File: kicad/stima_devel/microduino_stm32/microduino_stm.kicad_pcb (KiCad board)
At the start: 2 copper layers, 2 parts, among them IC1 STM32F103CBT6

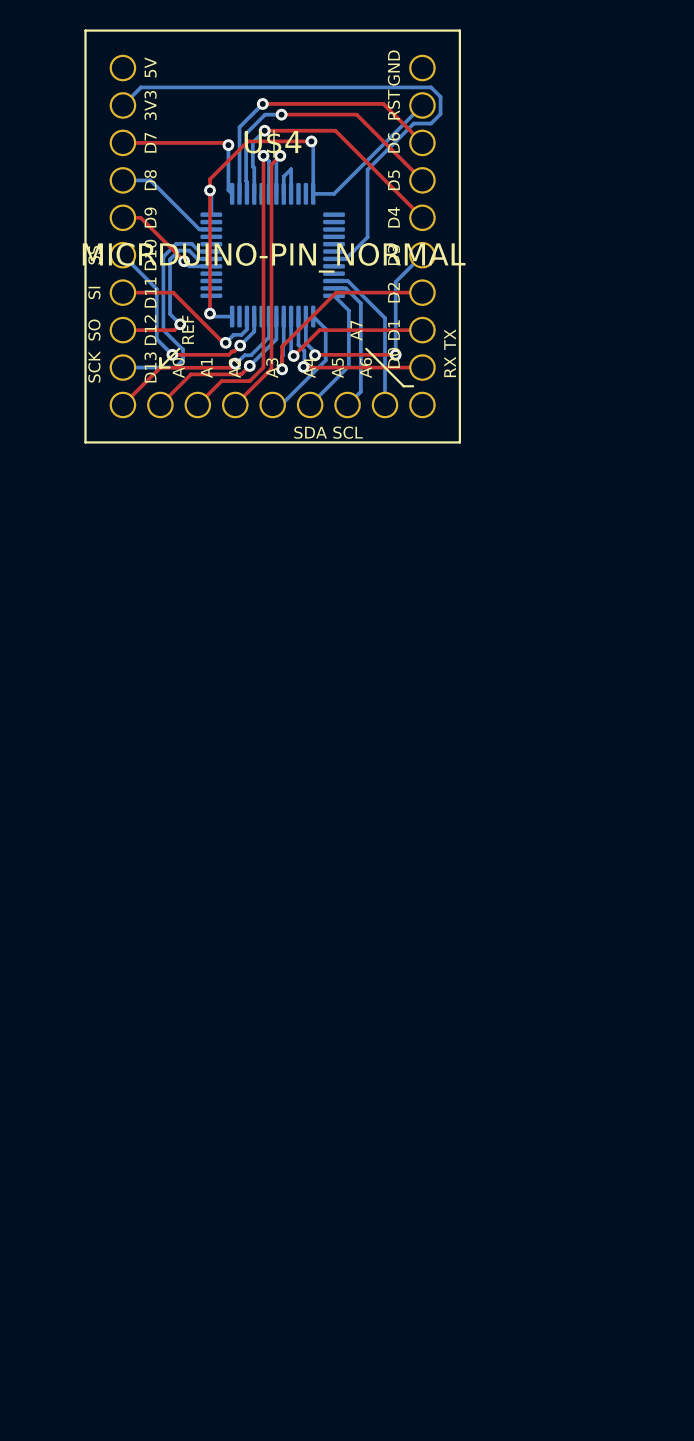
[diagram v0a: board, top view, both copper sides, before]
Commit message: Update schematic and testing partial routing
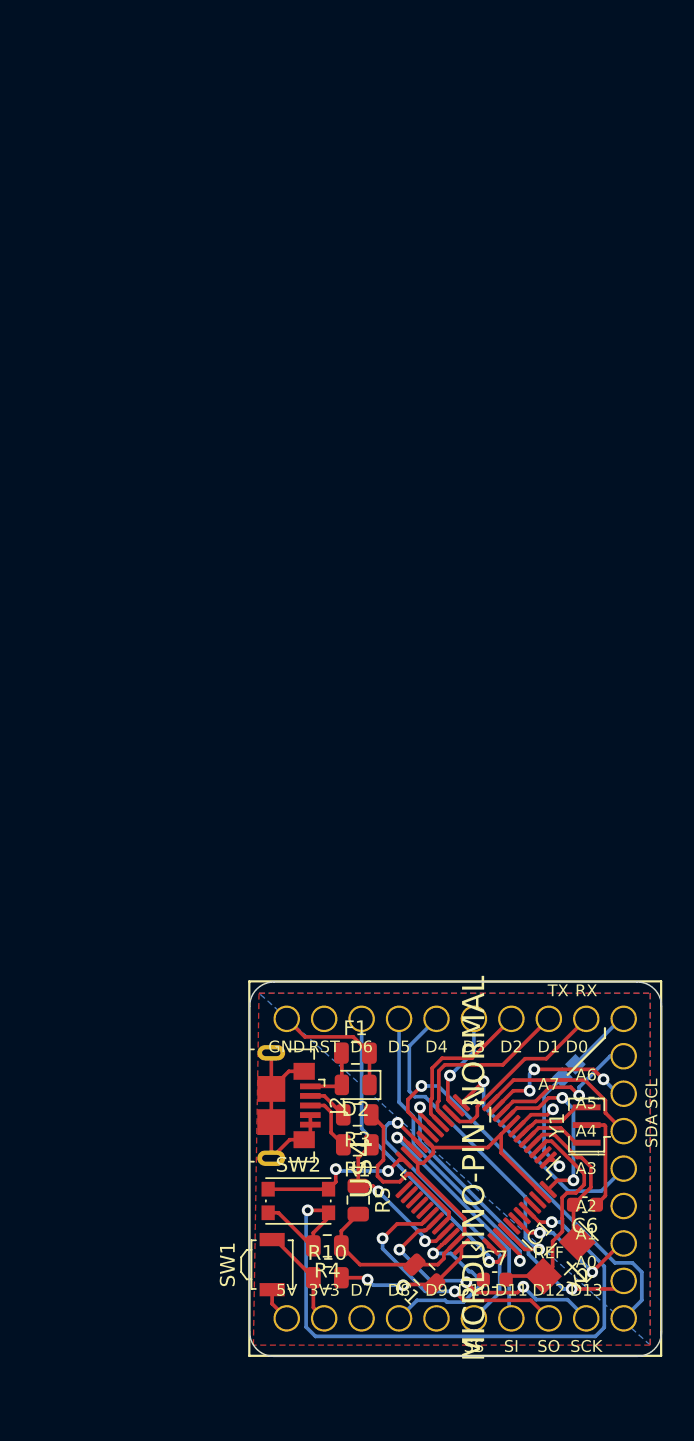
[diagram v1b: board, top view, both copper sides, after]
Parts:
- added C1: 10uF, Capacitor_SMD:C_0805_2012Metric, F.Cu at (158.8, 174.2)
- added C6: 10pF, Capacitor_SMD:C_0603_1608Metric, F.Cu at (169.7, 169.4)
- added C7: 10pF, Capacitor_SMD:C_0603_1608Metric, F.Cu at (163.6, 174.5)
- added D2: D, Diode_SMD:D_0805_2012Metric, F.Cu at (154.1, 161.3)
- added F1: 10uF, Capacitor_SMD:C_0805_2012Metric, F.Cu at (154.1, 159.1)
- added J1: Conn_01x01, TestPoint:TestPoint_Pad_1.0x1.0mm, B.Cu at (169.0, 159.9)
- added J2: USB_B_Micro, Connector_USB:USB_Micro-B_GCT_USB3076-30-A, F.Cu at (149.6, 162.7)
- added J3: Conn_01x01, TestPoint:TestPoint_Pad_1.0x1.0mm, B.Cu at (168.1, 160.8)
- added R1: 22, Capacitor_SMD:C_0805_2012Metric, F.Cu at (154.2, 165.4)
- added R10: 10k, Capacitor_SMD:C_0805_2012Metric, F.Cu at (152.2, 174.4)
- added R3: 22, Capacitor_SMD:C_0805_2012Metric, F.Cu at (154.2, 163.3)
- added R4: 10k, Capacitor_SMD:C_0805_2012Metric, F.Cu at (152.2, 172.2)
- added R5: 1.5k, Capacitor_SMD:C_0805_2012Metric, F.Cu at (154.3, 169.1)
- added SW1: SW_Push, Button_Switch_SMD:SW_SPST_B3U-3000P, F.Cu at (148.5, 173.5)
- added SW2: SW_Push, Button_Switch_SMD:SW_Push_1P1T_NO_CK_KMR2, F.Cu at (150.2, 169.2)
- added Y1: 8M, Crystal:Resonator_SMD_muRata_CSTxExxV-3Pin_3.0x1.1mm, F.Cu at (169.8, 164.0)
- added Y2: 32.768KHz, Crystal:Crystal_SMD_EuroQuartz_EQ161-2Pin_3.2x1.5mm_HandSoldering, F.Cu at (168.0, 173.1)
- IC1: moved to F.Cu
- moved IC1 63.9 mm to (162.3, 167.4), turned to 225 degrees
- moved U$4 63.4 mm to (162.2, 167.0), turned to 90 degrees
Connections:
- IC1 pad 2: Net-(IC1-Pad2) -> (no net)
- IC1 pad 25: Net-(IC1-Pad25) -> (no net)
- IC1 pad 26: Net-(IC1-Pad26) -> (no net)
- IC1 pad 27: Net-(IC1-Pad27) -> (no net)
- IC1 pad 28: Net-(IC1-Pad28) -> (no net)
- IC1 pad 29: /D4 -> (no net)
- IC1 pad 41: Net-(IC1-Pad41) -> (no net)
- IC1 pad 44: /32 -> Net-(IC1-Pad44)
- IC1 pad 45: /32 -> (no net)
- IC1 pad 46: /DISC -> (no net)
- U$4 pad 10: /N$13 -> /VBAT
- U$4 pad 23: /D4 -> (no net)
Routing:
- net GND: track 0.02 -> 57.4 mm
- net Net-(IC1-Pad44): track 0.00 -> 47.8 mm, vias 0 -> 2
- net /RST: track 37.5 -> 9.92 mm, vias 0 -> 1
- net /SDA: track 20.9 -> 0.00 mm, vias 1 -> 0
- net Net-(C7-Pad2): track 0.00 -> 15.4 mm
- net /A7: track 13.2 -> 28.1 mm
- net /SCL: track 22.6 -> 9.49 mm, vias 1 -> 2
- net /VBAT: track 0.00 -> 12.4 mm, vias 0 -> 1
- net /24_USBDM: track 0.00 -> 12.2 mm
- net /A6: track 11.3 -> 22.6 mm, vias 1 -> 2
- net /23_USBDP: track 0.00 -> 11.1 mm, vias 0 -> 2
- net Net-(C6-Pad2): track 0.00 -> 10.8 mm
- net /D6: track 10.6 -> 0.17 mm, vias 1 -> 0
- net /D10: track 15.9 -> 7.01 mm, vias 2 -> 1
- net +5V: track 0.00 -> 8.74 mm
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- added copper zone on B.Cu, net +3V3
- added copper zone on F.Cu, net GND
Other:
- board outline added: 27.9 x 25.4 mm

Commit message: pcb preview
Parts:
- moved C1 0.23 mm to (158.6, 174.0)
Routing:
- net /RST: track 9.92 -> 36.0 mm, vias 1 -> 4
- net /SDA: track 0.00 -> 13.4 mm, vias 0 -> 2
- net /D6: track 0.17 -> 11.5 mm, vias 0 -> 1
- net +3V3: track 32.7 -> 39.9 mm
- net GND: track 57.4 -> 64.3 mm, vias 0 -> 4
- net (no net): track 0.00 -> 3.30 mm
- net /D7: track 22.5 -> 24.5 mm, vias 1 -> 2
- net Net-(IC1-Pad44): track 47.8 -> 49.6 mm
- net /D5: track 12.6 -> 14.3 mm
- net /A7: track 28.1 -> 29.6 mm
- net /MOSI: track 10.8 -> 11.6 mm

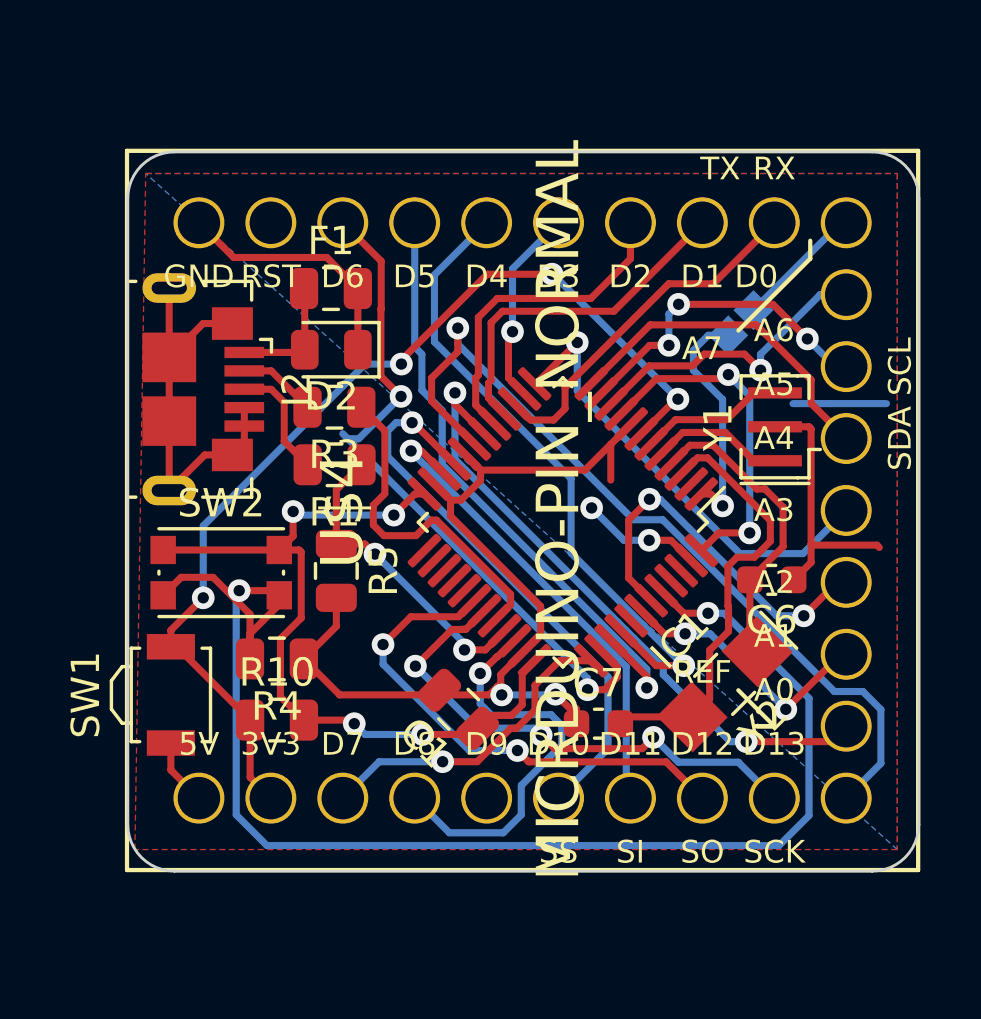
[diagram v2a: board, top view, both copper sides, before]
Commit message: pcb preview with corrections
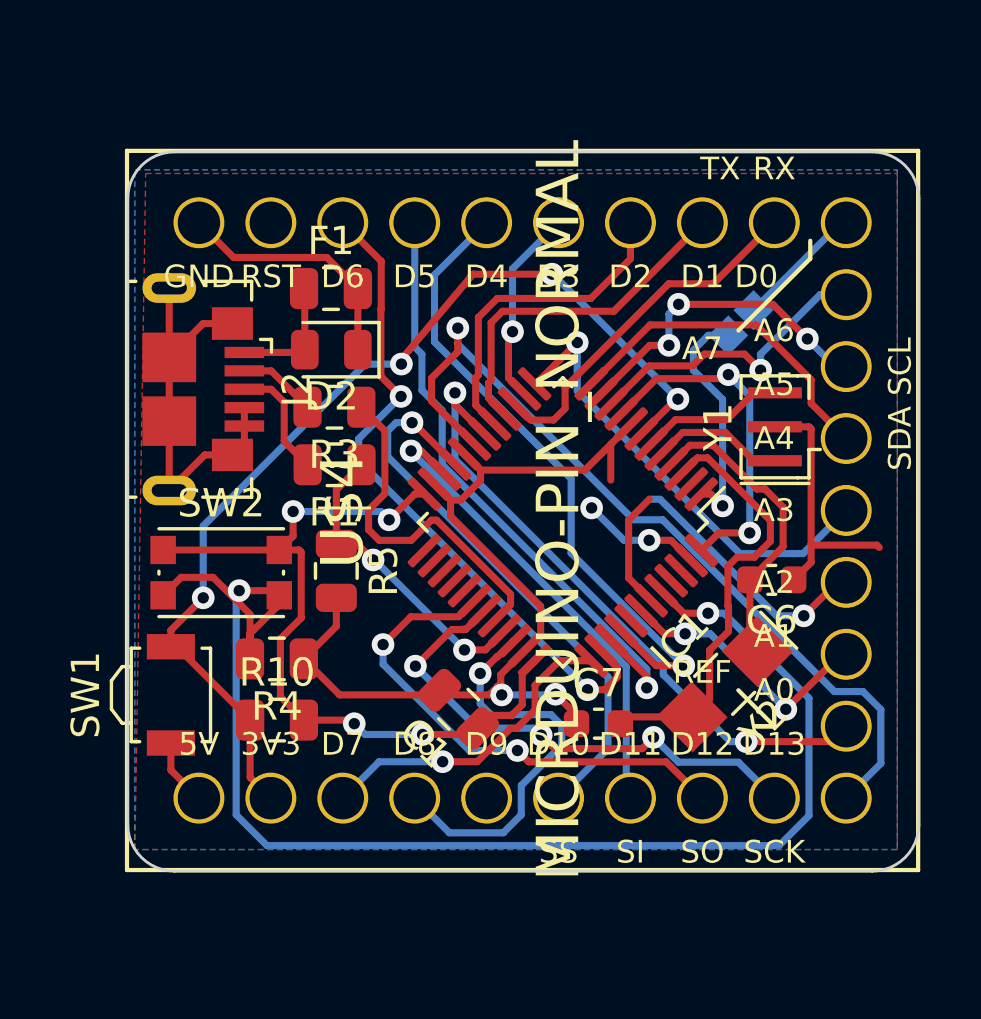
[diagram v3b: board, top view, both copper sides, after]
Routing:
- net (no net): track 3.30 -> 0.00 mm
- net /D7: track 24.5 -> 23.7 mm
- net GND: track 64.3 -> 63.7 mm
- net /SDA: vias 2 -> 1
